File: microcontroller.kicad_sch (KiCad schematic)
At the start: 20 parts, among them U4 RP2040, Y1 Crystal_GND24

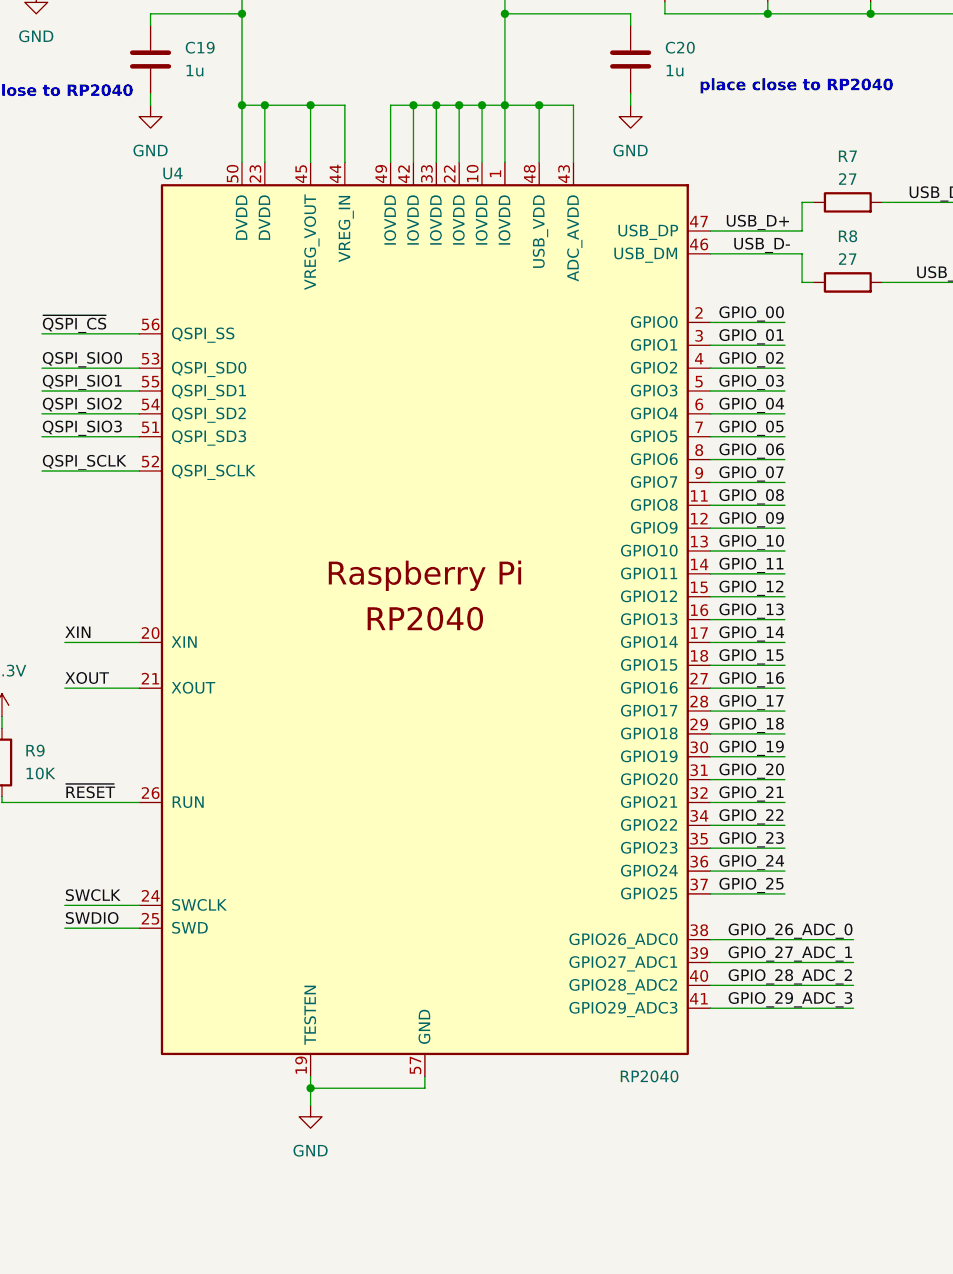
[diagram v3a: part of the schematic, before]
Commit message: Basic routing complete, rename
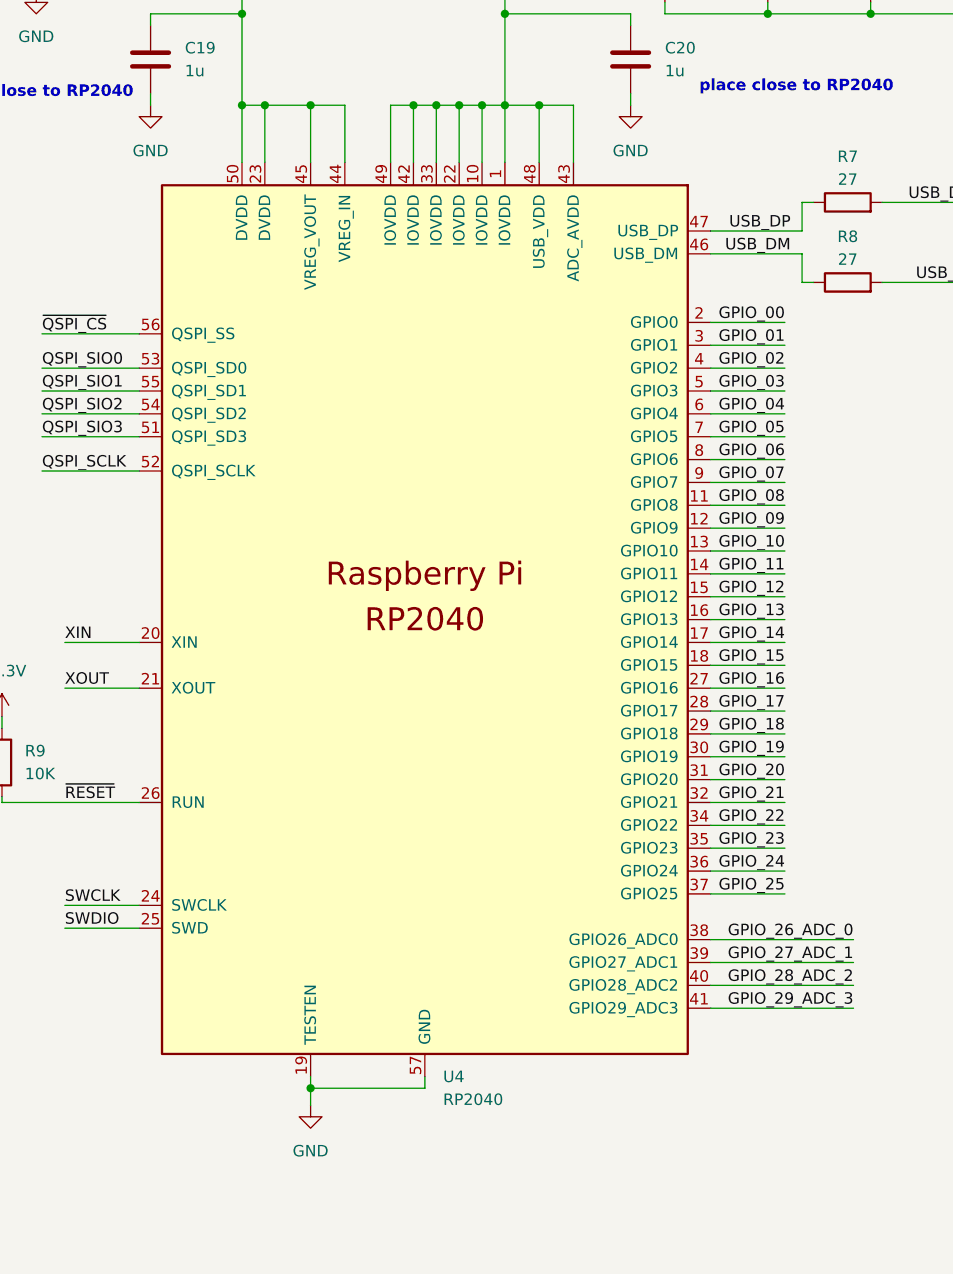
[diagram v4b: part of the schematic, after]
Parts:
- removed U4: RP2040, pico-card:RP2040-QFN-56, symbol pico-card:RP2040
- added U4: RP2040, Diva-Card:RP2040-QFN-56, symbol Diva-Card:RP2040
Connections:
- net +1V1: now also U4.23 (DVDD), U4.44 (VREG_IN), U4.45 (VREG_VOUT), U4.50 (DVDD)
- net +3V3: now also U4.1 (IOVDD), U4.10 (IOVDD), U4.22 (IOVDD), U4.33 (IOVDD), U4.42 (IOVDD), U4.43 (ADC_AVDD), U4.48 (USB_VDD), U4.49 (IOVDD)
- net GND: now also U4.19 (TESTEN), U4.57 (GND)
- net GPIO_00: now also U4.2 (GPIO0)
- net GPIO_01: now also U4.3 (GPIO1)
- net GPIO_02: now also U4.4 (GPIO2)
- net GPIO_03: now also U4.5 (GPIO3)
- net GPIO_04: now also U4.6 (GPIO4)
- net GPIO_05: now also U4.7 (GPIO5)
- net GPIO_06: now also U4.8 (GPIO6)
- net GPIO_07: now also U4.9 (GPIO7)
- net GPIO_08: now also U4.11 (GPIO8)
- net GPIO_09: now also U4.12 (GPIO9)
- net GPIO_10: now also U4.13 (GPIO10)
- net GPIO_11: now also U4.14 (GPIO11)
- net GPIO_12: now also U4.15 (GPIO12)
- net GPIO_13: now also U4.16 (GPIO13)
- net GPIO_14: now also U4.17 (GPIO14)
- net GPIO_15: now also U4.18 (GPIO15)
- net GPIO_16: now also U4.27 (GPIO16)
- net GPIO_17: now also U4.28 (GPIO17)
- net GPIO_18: now also U4.29 (GPIO18)
- net GPIO_19: now also U4.30 (GPIO19)
- net GPIO_20: now also U4.31 (GPIO20)
- net GPIO_21: now also U4.32 (GPIO21)
- net GPIO_22: now also U4.34 (GPIO22)
- net GPIO_23: now also U4.35 (GPIO23)
- net GPIO_24: now also U4.36 (GPIO24)
- net GPIO_25: now also U4.37 (GPIO25)
- net GPIO_26_ADC_0: now also U4.38 (GPIO26_ADC0)
- net GPIO_27_ADC_1: now also U4.39 (GPIO27_ADC1)
- net GPIO_28_ADC_2: now also U4.40 (GPIO28_ADC2)
- net GPIO_29_ADC_3: now also U4.41 (GPIO29_ADC3)
- net QSPI_SCLK: now also U4.52 (QSPI_SCLK)
- net QSPI_SIO0: now also U4.53 (QSPI_SD0)
- net QSPI_SIO1: now also U4.55 (QSPI_SD1)
- net QSPI_SIO2: now also U4.54 (QSPI_SD2)
- net QSPI_SIO3: now also U4.51 (QSPI_SD3)
- net SWCLK: now also U4.24 (SWCLK)
- net SWDIO: now also U4.25 (SWD)
- net USB_D+: no longer R7.1
- net USB_D-: no longer R8.1
- net XIN: now also U4.20 (XIN)
- net XOUT: now also U4.21 (XOUT)
- net ~{QSPI_CS}: now also U4.56 (QSPI_SS)
- net ~{RESET}: now also U4.26 (RUN)
- new net USB_DM: R8.1, U4.46 (USB_DM)
- new net USB_DP: R7.1, U4.47 (USB_DP)

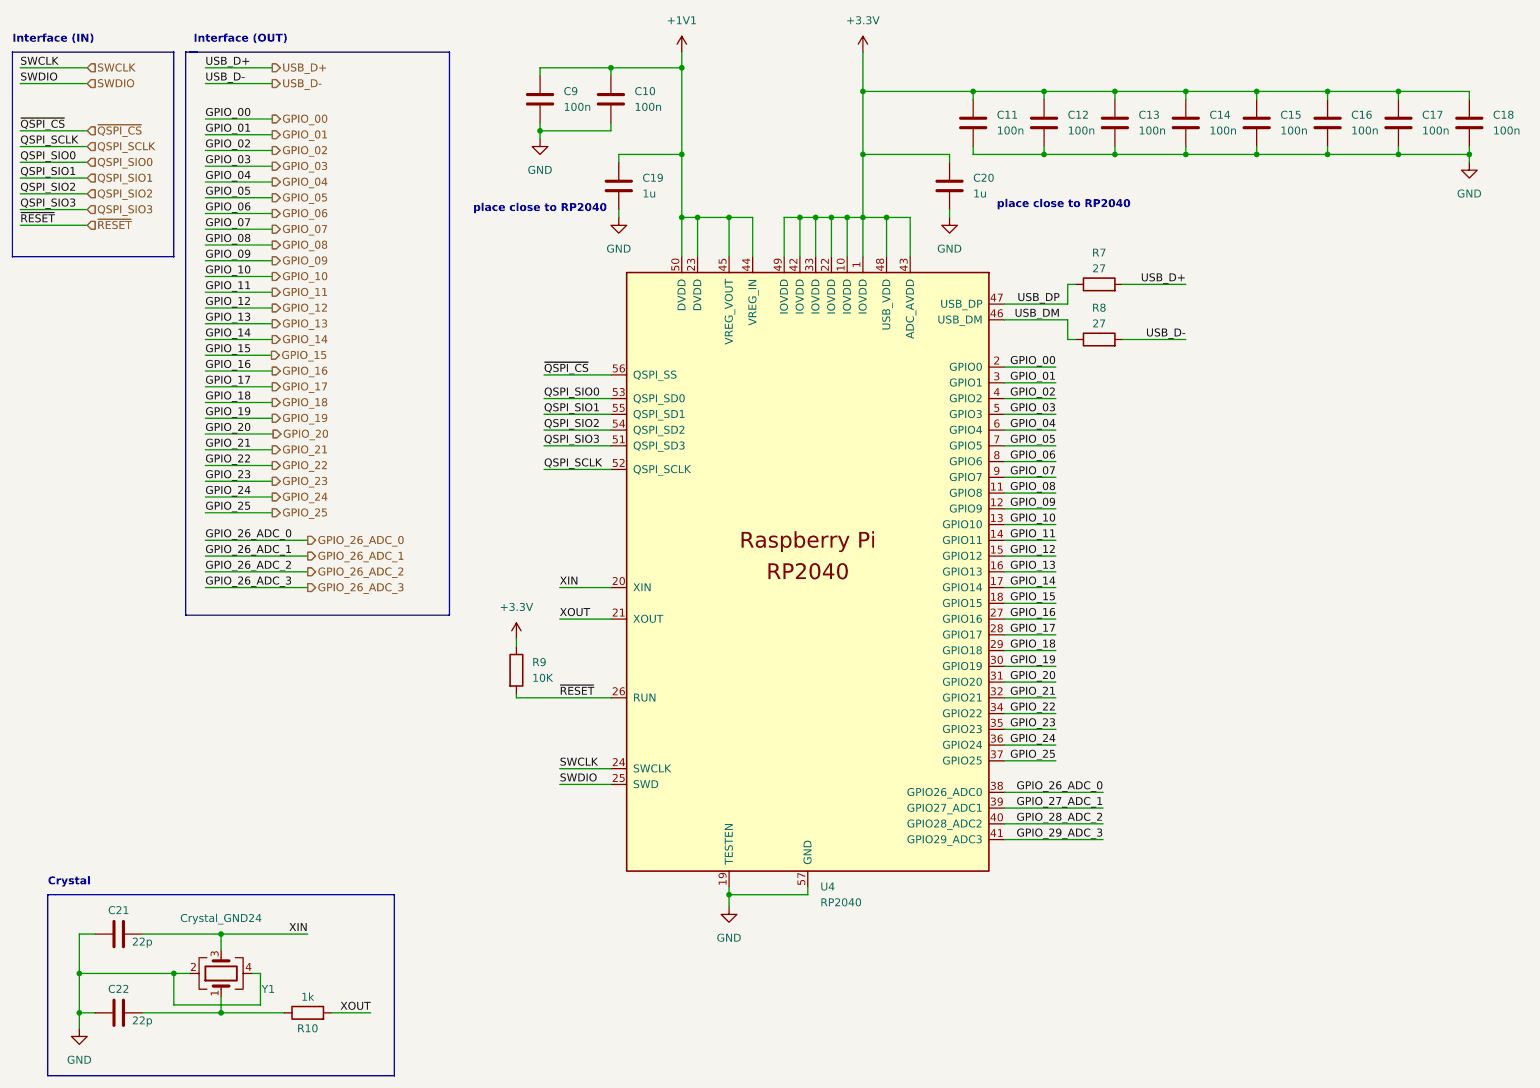
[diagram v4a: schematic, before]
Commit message: Adding schematic pdf
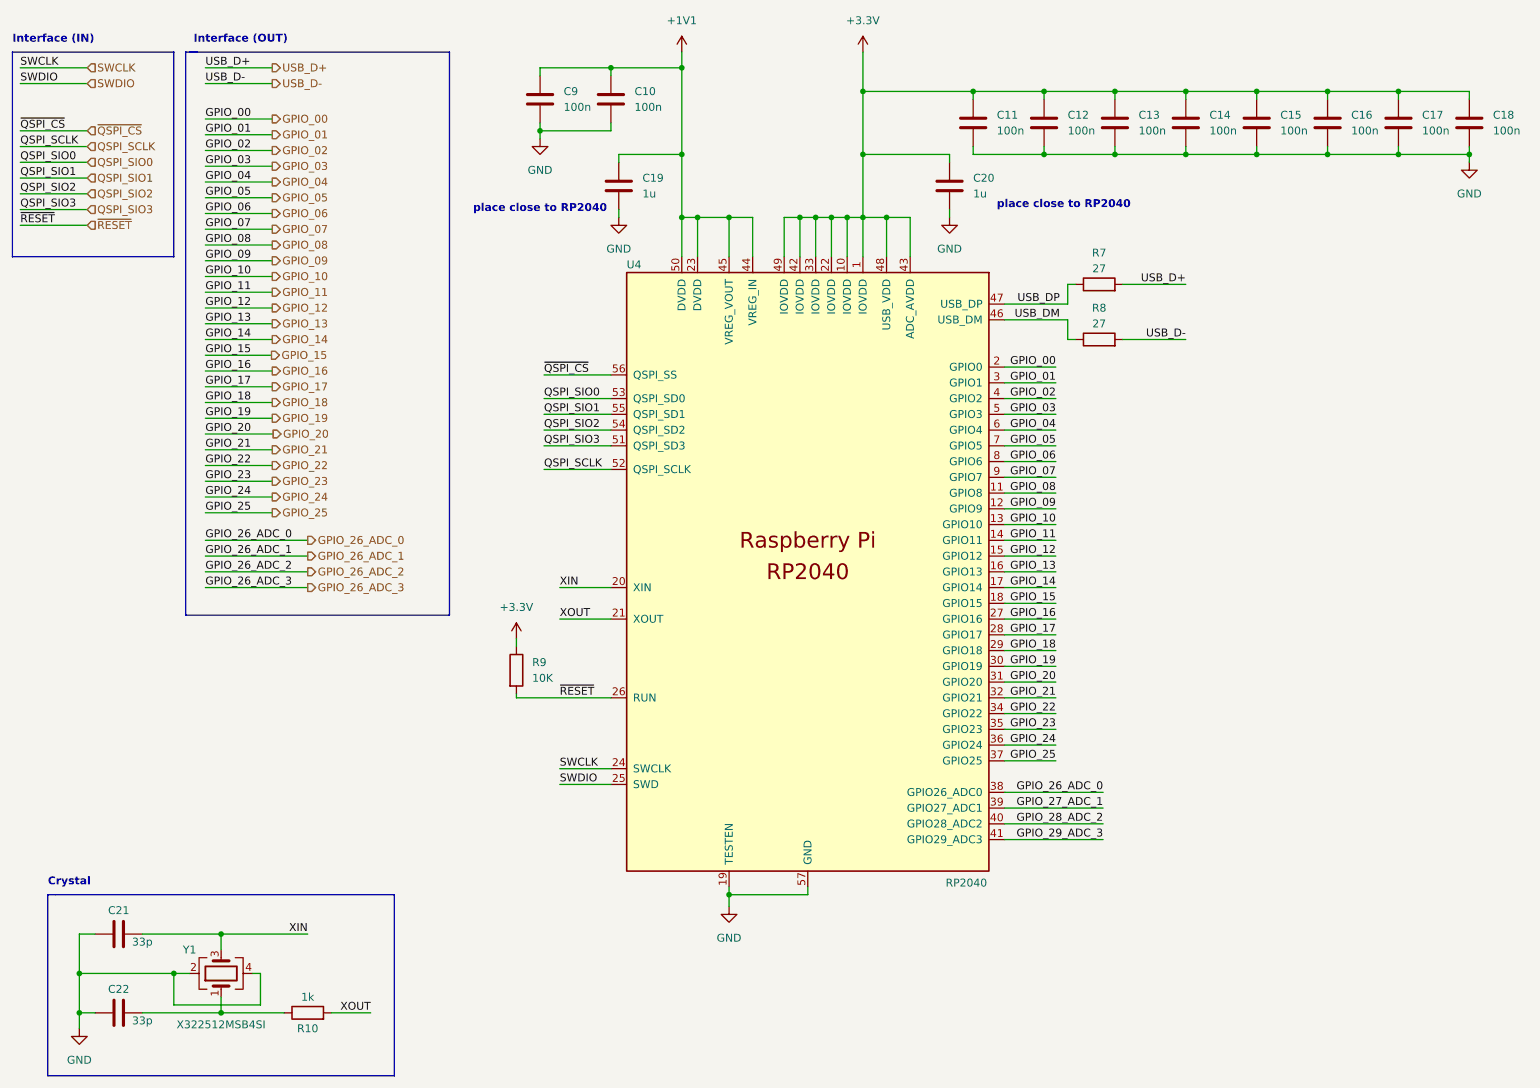
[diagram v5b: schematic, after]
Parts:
- C21, C22: value 22p -> 33p
- Y1: value Crystal_GND24 -> X322512MSB4SI
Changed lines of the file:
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@@
   (symbol (lib_id "Device:Crystal_GND24") (at 48.895 173.99 90) (unit 1)
     (in_bom yes) (on_board yes)
-    (property "Reference" "Y1" (id 0) (at 56.515 176.53 90))
-    (property "Value" "Crystal_GND24" (id 1) (at 48.895 165.1 90))
+    (property "Reference" "Y1" (id 0) (at 43.815 170.18 90))
+    (property "Value" "X322512MSB4SI" (id 1) (at 48.895 182.245 90))
     (property "Footprint" "Crystal:Crystal_SMD_3225-4Pin_3.2x2.5mm" (id 2) (at 48.895 173.99 0)
       (effects (font (size 1.27 1.27)) hide)
@@
   )
   (symbol (lib_id "Diva-Card:RP2040") (at 143.51 109.22 0) (unit 1)
-    (in_bom yes) (on_board yes) (fields_autoplaced)
-    (property "Reference" "U4" (id 0) (at 145.5294 160.02 0)
+    (in_bom yes) (on_board yes)
+    (property "Reference" "U4" (id 0) (at 114.3 59.69 0)
       (effects (font (size 1.27 1.27)) (justify left))
     )
-    (property "Value" "RP2040" (id 1) (at 145.5294 162.56 0)
+    (property "Value" "RP2040" (id 1) (at 165.735 159.385 0)
       (effects (font (size 1.27 1.27)) (justify left))
     )
@@
     (in_bom yes) (on_board yes)
     (property "Reference" "C21" (id 0) (at 32.385 163.83 90))
-    (property "Value" "22p" (id 1) (at 36.195 168.91 90))
+    (property "Value" "33p" (id 1) (at 36.195 168.91 90))
     (property "Footprint" "Capacitor_SMD:C_0402_1005Metric" (id 2) (at 36.195 166.6748 0)
       (effects (font (size 1.27 1.27)) hide)
@@
     (in_bom yes) (on_board yes)
     (property "Reference" "C22" (id 0) (at 32.385 176.53 90))
-    (property "Value" "22p" (id 1) (at 36.195 181.61 90))
+    (property "Value" "33p" (id 1) (at 36.195 181.61 90))
     (property "Footprint" "Capacitor_SMD:C_0402_1005Metric" (id 2) (at 36.195 179.3748 0)
       (effects (font (size 1.27 1.27)) hide)
